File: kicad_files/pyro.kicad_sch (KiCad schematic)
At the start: 14 parts, among them J10 IGN_2, J9 IGN_1, Q1 AO3400A, Q2 AO3400A

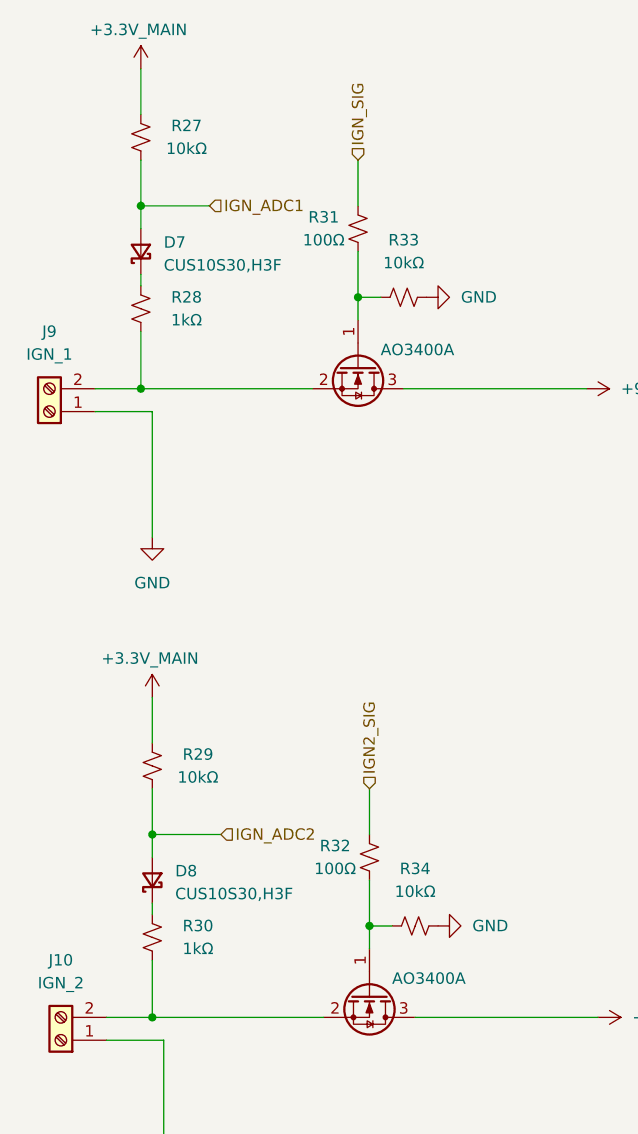
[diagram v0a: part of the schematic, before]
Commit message: size polyfuse, final drc stuff
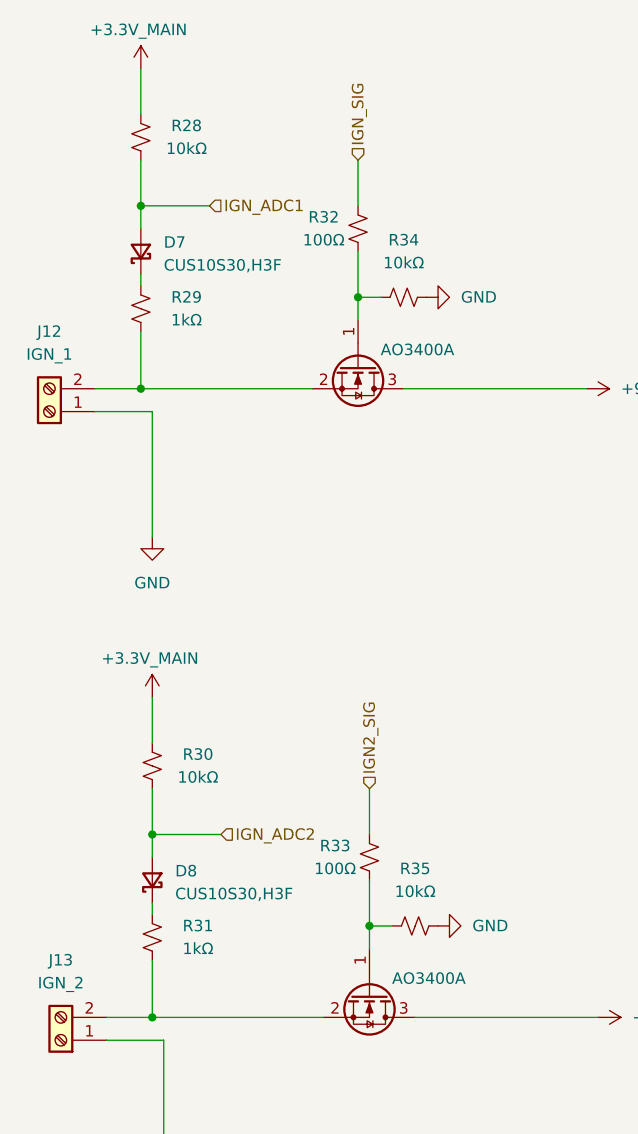
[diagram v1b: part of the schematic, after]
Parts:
- renumbered J9 to J12, J10 to J13, R27 to R28, R28 to R29, R29 to R30, R30 to R31, R31 to R32, R32 to R33, R33 to R34, R34 to R35
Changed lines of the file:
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@@
 		(in_pos_files yes)
 		(dnp no)
-		(property "Reference" "R27"
+		(property "Reference" "R28"
 			(at 140.97 40.64 0)
 			(show_name no)
@@
 			(project "versorlite"
 				(path "/1a230af0-0a74-48f7-8607-b087121dda49/f02bd2f9-723f-45ac-a652-42be6cba2a93"
-					(reference "R27")
+					(reference "R28")
 					(unit 1)
 				)
@@
 		(dnp no)
 		(fields_autoplaced yes)
-		(property "Reference" "#PWR097"
+		(property "Reference" "#PWR098"
 			(at 173.99 59.69 0)
 			(hide yes)
@@
 			(project "versorlite"
 				(path "/1a230af0-0a74-48f7-8607-b087121dda49/f02bd2f9-723f-45ac-a652-42be6cba2a93"
-					(reference "#PWR097")
+					(reference "#PWR098")
 					(unit 1)
 				)
@@
 		(dnp no)
 		(fields_autoplaced yes)
-		(property "Reference" "J10"
+		(property "Reference" "J13"
 			(at 127 133.35 0)
 			(show_name no)
@@
 			(project "versorlite"
 				(path "/1a230af0-0a74-48f7-8607-b087121dda49/f02bd2f9-723f-45ac-a652-42be6cba2a93"
-					(reference "J10")
+					(reference "J13")
 					(unit 1)
 				)
@@
 		(dnp no)
 		(fields_autoplaced yes)
-		(property "Reference" "#PWR096"
+		(property "Reference" "#PWR097"
 			(at 138.43 162.56 0)
 			(hide yes)
@@
 			(project "versorlite"
 				(path "/1a230af0-0a74-48f7-8607-b087121dda49/f02bd2f9-723f-45ac-a652-42be6cba2a93"
-					(reference "#PWR096")
+					(reference "#PWR097")
 					(unit 1)
 				)
@@
 		(dnp no)
 		(fields_autoplaced yes)
-		(property "Reference" "#PWR099"
+		(property "Reference" "#PWR0100"
 			(at 181.61 69.85 0)
 			(hide yes)
@@
 			(project "versorlite"
 				(path "/1a230af0-0a74-48f7-8607-b087121dda49/f02bd2f9-723f-45ac-a652-42be6cba2a93"
-					(reference "#PWR099")
+					(reference "#PWR0100")
 					(unit 1)
 				)
@@
 		(in_pos_files yes)
 		(dnp no)
-		(property "Reference" "R30"
+		(property "Reference" "R31"
 			(at 142.24 129.54 0)
 			(show_name no)
@@
 			(project "versorlite"
 				(path "/1a230af0-0a74-48f7-8607-b087121dda49/f02bd2f9-723f-45ac-a652-42be6cba2a93"
-					(reference "R30")
+					(reference "R31")
 					(unit 1)
 				)
@@
 		(dnp no)
 		(fields_autoplaced yes)
-		(property "Reference" "#PWR094"
+		(property "Reference" "#PWR095"
 			(at 137.16 92.71 0)
 			(hide yes)
@@
 			(project "versorlite"
 				(path "/1a230af0-0a74-48f7-8607-b087121dda49/f02bd2f9-723f-45ac-a652-42be6cba2a93"
-					(reference "#PWR094")
+					(reference "#PWR095")
 					(unit 1)
 				)
@@
 		(in_pos_files yes)
 		(dnp no)
-		(property "Reference" "#PWR093"
+		(property "Reference" "#PWR094"
 			(at 135.89 38.1 0)
 			(hide yes)
@@
 			(project "versorlite"
 				(path "/1a230af0-0a74-48f7-8607-b087121dda49/f02bd2f9-723f-45ac-a652-42be6cba2a93"
-					(reference "#PWR093")
+					(reference "#PWR094")
 					(unit 1)
 				)
@@
 		(dnp no)
 		(fields_autoplaced yes)
-		(property "Reference" "#PWR098"
+		(property "Reference" "#PWR099"
 			(at 175.26 129.54 0)
 			(hide yes)
@@
 			(project "versorlite"
 				(path "/1a230af0-0a74-48f7-8607-b087121dda49/f02bd2f9-723f-45ac-a652-42be6cba2a93"
-					(reference "#PWR098")
+					(reference "#PWR099")
 					(unit 1)
 				)
@@
 		(in_pos_files yes)
 		(dnp no)
-		(property "Reference" "#PWR095"
+		(property "Reference" "#PWR096"
 			(at 137.16 107.95 0)
 			(hide yes)
@@
 			(project "versorlite"
 				(path "/1a230af0-0a74-48f7-8607-b087121dda49/f02bd2f9-723f-45ac-a652-42be6cba2a93"
-					(reference "#PWR095")
+					(reference "#PWR096")
 					(unit 1)
 				)
@@
 		(in_pos_files yes)
 		(dnp no)
-		(property "Reference" "R32"
+		(property "Reference" "R33"
 			(at 157.48 120.65 0)
 			(show_name no)
@@
 			(project "versorlite"
 				(path "/1a230af0-0a74-48f7-8607-b087121dda49/f02bd2f9-723f-45ac-a652-42be6cba2a93"
-					(reference "R32")
+					(reference "R33")
 					(unit 1)
 				)
@@
 		(dnp no)
 		(fields_autoplaced yes)
-		(property "Reference" "J9"
+		(property "Reference" "J12"
 			(at 125.73 63.5 0)
 			(show_name no)
@@
 			(project "versorlite"
 				(path "/1a230af0-0a74-48f7-8607-b087121dda49/f02bd2f9-723f-45ac-a652-42be6cba2a93"
-					(reference "J9")
+					(reference "J12")
 					(unit 1)
 				)
@@
 		(in_pos_files yes)
 		(dnp no)
-		(property "Reference" "R29"
+		(property "Reference" "R30"
 			(at 142.24 110.49 0)
 			(show_name no)
@@
 			(project "versorlite"
 				(path "/1a230af0-0a74-48f7-8607-b087121dda49/f02bd2f9-723f-45ac-a652-42be6cba2a93"
-					(reference "R29")
+					(reference "R30")
 					(unit 1)
 				)
@@
 		(in_pos_files yes)
 		(dnp no)
-		(property "Reference" "R34"
+		(property "Reference" "R35"
 			(at 166.37 123.19 90)
 			(show_name no)
@@
 			(project "versorlite"
 				(path "/1a230af0-0a74-48f7-8607-b087121dda49/f02bd2f9-723f-45ac-a652-42be6cba2a93"
-					(reference "R34")
+					(reference "R35")
 					(unit 1)
 				)
@@
 		(in_pos_files yes)
 		(dnp no)
-		(property "Reference" "R28"
+		(property "Reference" "R29"
 			(at 140.97 59.69 0)
 			(show_name no)
@@
 			(project "versorlite"
 				(path "/1a230af0-0a74-48f7-8607-b087121dda49/f02bd2f9-723f-45ac-a652-42be6cba2a93"
-					(reference "R28")
+					(reference "R29")
 					(unit 1)
 				)
@@
 		(dnp no)
 		(fields_autoplaced yes)
-		(property "Reference" "#PWR0100"
+		(property "Reference" "#PWR0101"
 			(at 182.88 139.7 0)
 			(hide yes)
@@
 			(project "versorlite"
 				(path "/1a230af0-0a74-48f7-8607-b087121dda49/f02bd2f9-723f-45ac-a652-42be6cba2a93"
-					(reference "#PWR0100")
+					(reference "#PWR0101")
 					(unit 1)
 				)
@@
 		(in_pos_files yes)
 		(dnp no)
-		(property "Reference" "R33"
+		(property "Reference" "R34"
 			(at 165.1 53.34 90)
 			(show_name no)
@@
 			(project "versorlite"
 				(path "/1a230af0-0a74-48f7-8607-b087121dda49/f02bd2f9-723f-45ac-a652-42be6cba2a93"
-					(reference "R33")
+					(reference "R34")
 					(unit 1)
 				)
@@
 		(in_pos_files yes)
 		(dnp no)
-		(property "Reference" "R31"
+		(property "Reference" "R32"
 			(at 156.21 50.8 0)
 			(show_name no)
@@
 			(project "versorlite"
 				(path "/1a230af0-0a74-48f7-8607-b087121dda49/f02bd2f9-723f-45ac-a652-42be6cba2a93"
-					(reference "R31")
-					(unit 1)
-				)
+					(reference "R32")
+					(unit 1)
+				)

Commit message: fix ign
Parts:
- removed R32, R33: 100Ω, Resistor_SMD:R_0603_1608Metric, symbol Device:R_Small_US
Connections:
- net +9V: now also J12.2 (Pin_2), J13.2 (Pin_2), R29.2, R31.2; no longer Q1.3 (D), Q2.3 (D)
- net GND: now also Q1.2 (S), Q2.2 (S); no longer J12.1 (Pin_1), J13.1 (Pin_1)
- net IGN2_SIG: now also Q2.1 (G), R35.1
- net IGN_SIG: now also Q1.1 (G), R34.1
- new net: J13.1 (Pin_1), Q2.3 (D)
- new net: J12.1 (Pin_1), Q1.3 (D)
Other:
- moved on the sheet: R34, R35

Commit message: fix pyro adc
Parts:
- removed D7, D8: CUS10S30,H3F, Diode_SMD:D_SOD-323, symbol Device:D_Schottky_Small
- removed R30: 10kΩ, Resistor_SMD:R_0402_1005Metric, symbol Device:R_Small_US
- added R33: 10kΩ, Resistor_SMD:R_0402_1005Metric, symbol Device:R_Small_US
- added R34: 1kΩ, Resistor_SMD:R_0402_1005Metric, symbol Device:R_Small_US
- added R35: 5.6kΩ, Resistor_SMD:R_0402_1005Metric, symbol Device:R_Small_US
- R30: renamed from R29; footprint Resistor_SMD:R_0805_2012Metric -> Resistor_SMD:R_0402_1005Metric
- R31: value 1kΩ -> 5.6kΩ; footprint Resistor_SMD:R_0805_2012Metric -> Resistor_SMD:R_0402_1005Metric
- renumbered J12 to J11, J13 to J12, R34 to R28, R28 to R29, R35 to R32
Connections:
- net +3.3V_MAIN is gone; now on an unnamed net: R29.1
- net +9V: no longer R30.2, R31.2
- net GND: now also R31.2, R35.2
- net IGN_ADC1: now also R30.1; no longer R29.2
- net IGN_ADC2: now also R34.1
- net at J12.1 (Pin_1), Q2.3 (D): now also R33.1
- net at R31.1: now also R29.2, R30.2
- new net: R33.2, R34.2, R35.1
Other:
- moved on the sheet: J12, R28, R29, R30, R32

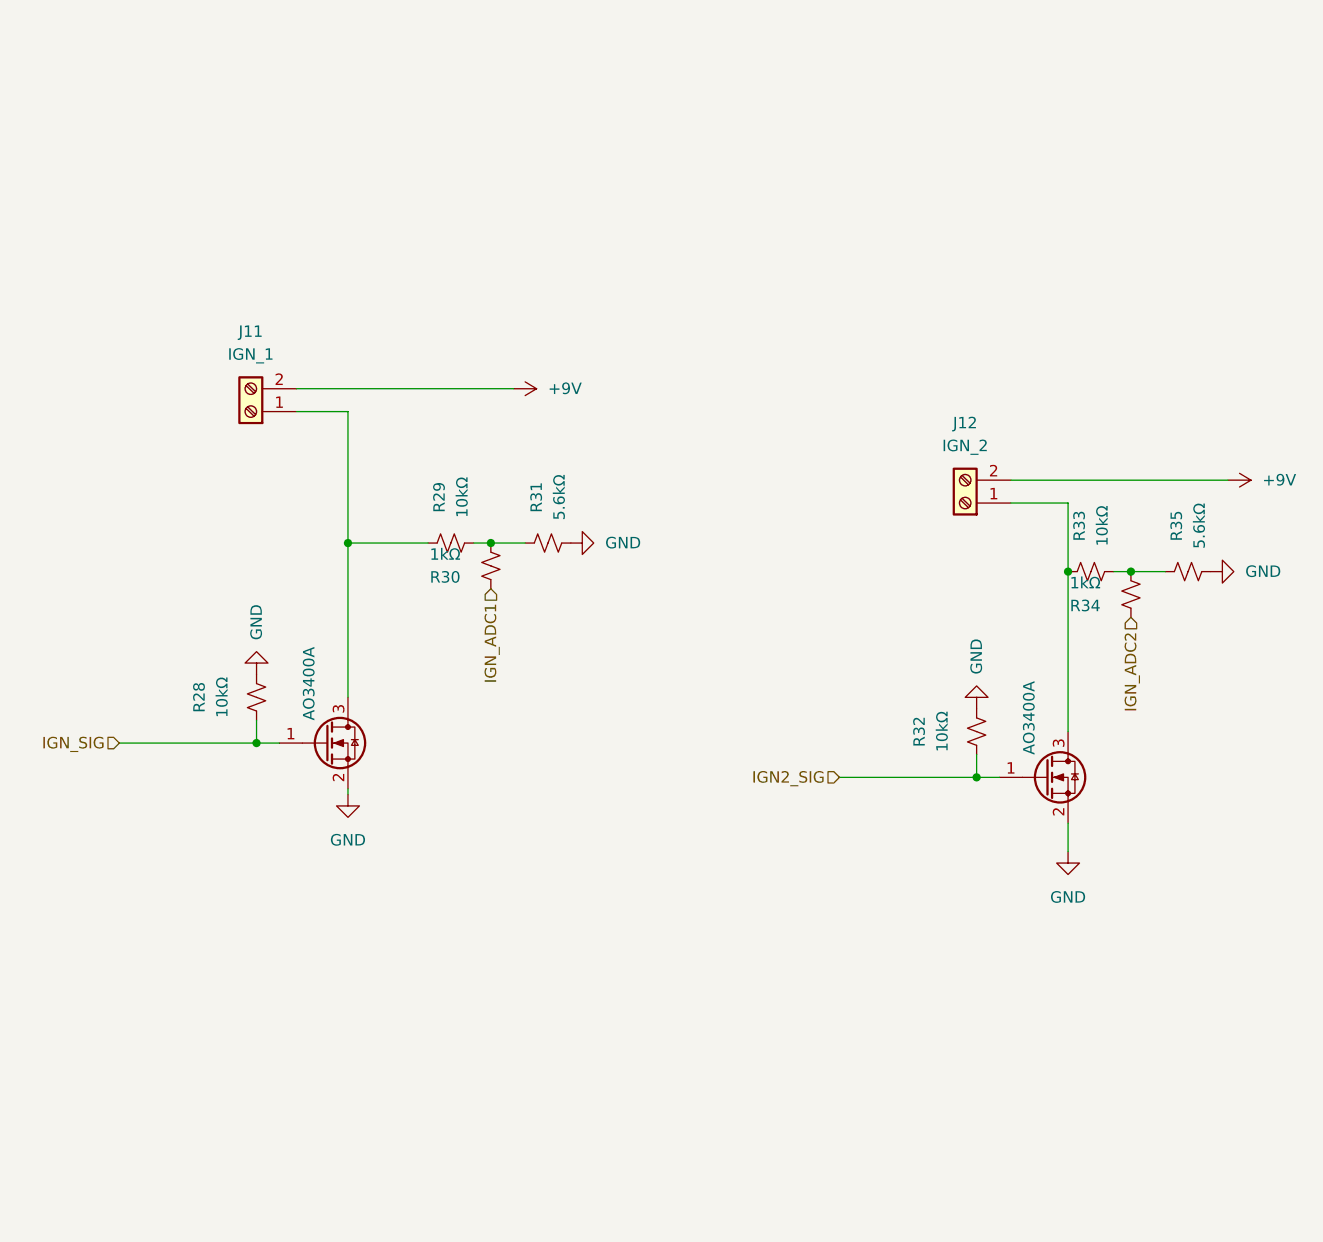
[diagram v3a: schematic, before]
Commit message: fix pyro channel
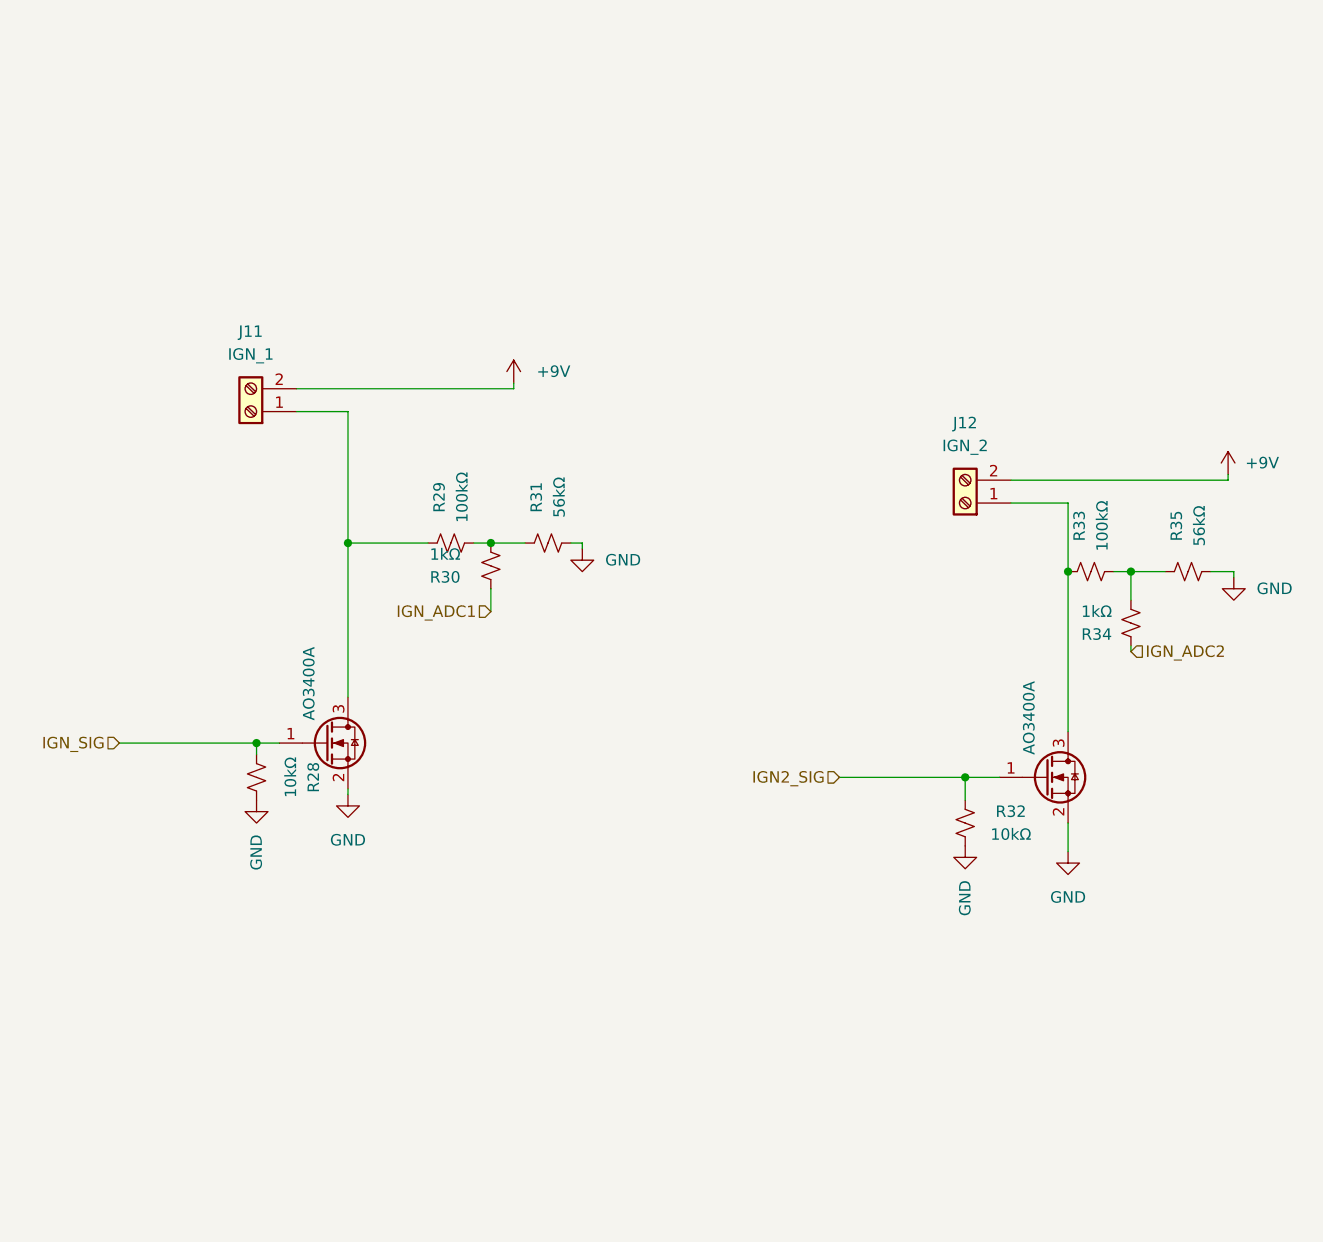
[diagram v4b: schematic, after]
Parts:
- R29, R33: value 10kΩ -> 100kΩ
- R31, R35: value 5.6kΩ -> 56kΩ
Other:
- moved on the sheet: R28, R32, R34
